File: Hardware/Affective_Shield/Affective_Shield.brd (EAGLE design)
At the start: 70 x 55 mm, 17 parts

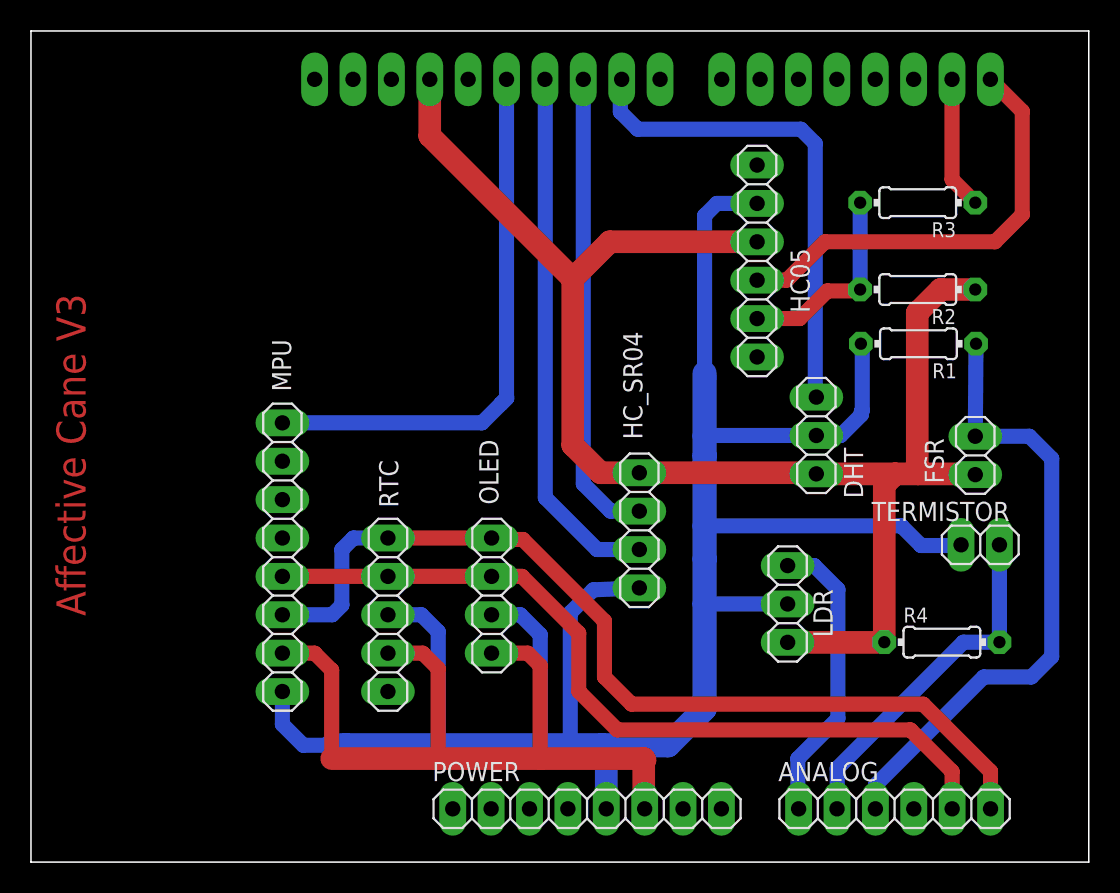
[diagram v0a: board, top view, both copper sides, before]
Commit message: Add Oximetry and GPS
Oximetry sensor added. GPS added
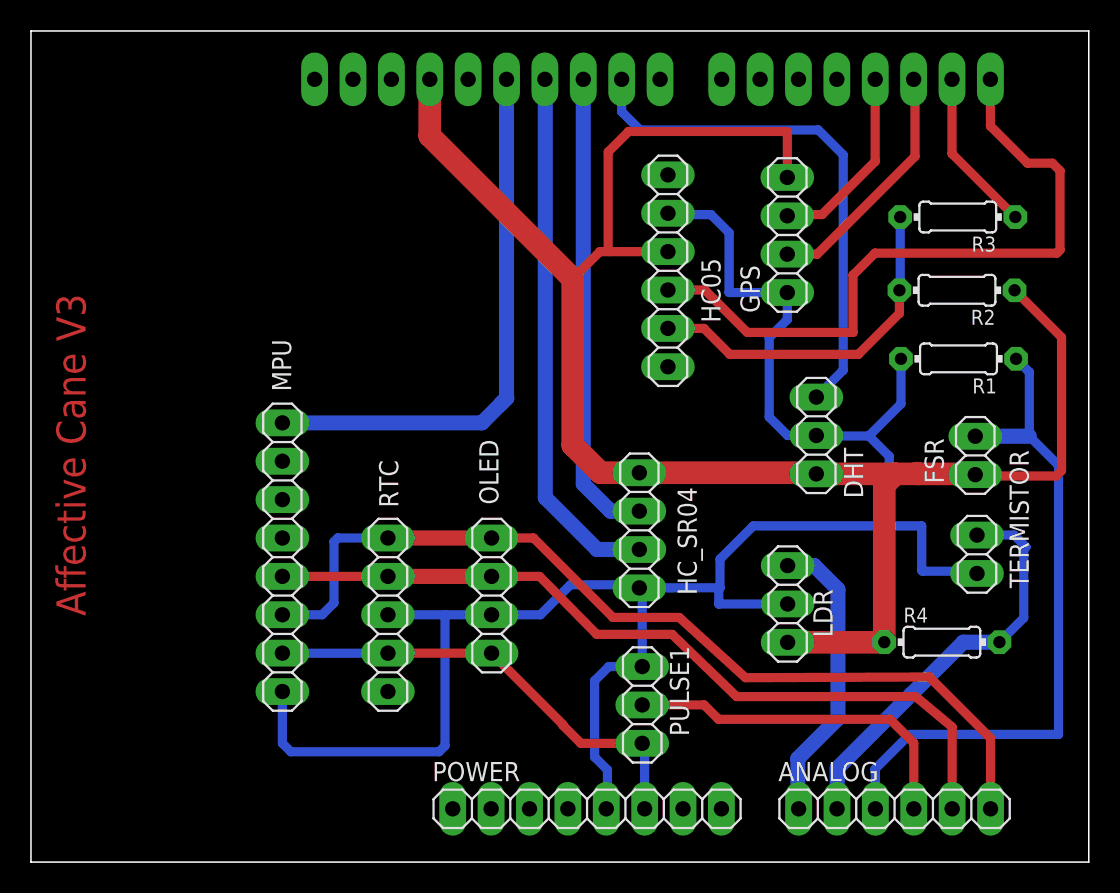
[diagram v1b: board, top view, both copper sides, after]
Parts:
- added GPS: GPS, pinhead:1X04
- added PULSE1: pulse_sensor, pinhead:1X03
- moved HC05 5.94 mm to (42.2, 38.1)
- moved R1 2.83 mm to (61.4, 32.3)
- moved R3 2.82 mm to (61.3, 41.7)
- moved R2 2.60 mm to (61.3, 36.8)
- moved TERMISTOR 0.66 mm to (62.6, 19.4), turned to 90 degrees
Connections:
- new net A3: ANALOG.4, PULSE1.2
- new net RX_GPS: GPS.2, JP1.3
- new net TX_GPS: GPS.3, JP1.4
- net +5V: now also GPS.1, PULSE1.1
- net GND1: now also PULSE1.3
- net GND2: now also GPS.4
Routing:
- net A3: track 0.00 -> 23.4 mm
- net GND1: track 53.3 -> 30.7 mm
- net GND2: track 101.8 -> 121.8 mm
- net +5V: track 150.6 -> 133.0 mm
- net RX: track 29.2 -> 45.8 mm
- net RX_GPS: track 0.00 -> 16.3 mm
- net TX_GPS: track 0.00 -> 12.7 mm
- net N$3: track 13.4 -> 23.5 mm
- net A1: track 23.3 -> 27.5 mm
- net A2: track 41.6 -> 45.3 mm
- net D09: track 32.8 -> 34.8 mm
- net TX: track 8.80 -> 10.8 mm
- net A4: track 54.4 -> 53.7 mm
- net A5: track 62.2 -> 61.6 mm

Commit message: shield corrective update: Changed some ports, and adapted to only bottom solder on components
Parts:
- removed R4: 10KR, resistor:0204/7
- removed TERMISTOR: TERMISTOR, pinhead:1X02
- added GSR_: GROOVE, pinhead:1X04
- moved LDR 2.02 mm to (51.9, 16.9), turned to 90 degrees
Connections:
- net +5V: now also GSR_.3; no longer TERMISTOR.1
- net A1: now also GSR_.1; no longer R4.2, TERMISTOR.2
- net A4: now also OLED.4; no longer OLED.3
- net A5: now also OLED.3; no longer OLED.4
- net GND1: now also GSR_.4
- net GND2: no longer R4.1
- net N$3: now also HC05.4; no longer HC05.5
- net RX: now also HC05.5; no longer HC05.4
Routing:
- net A5: track 61.6 -> 103.6 mm, vias 0 -> 3
- net GND1: track 30.7 -> 69.6 mm
- net GND2: track 121.8 -> 152.4 mm, vias 0 -> 4
- net +5V: track 133.0 -> 154.9 mm, vias 0 -> 5
- net A1: track 27.5 -> 17.1 mm
- net RX: track 45.8 -> 37.3 mm, vias 0 -> 2
- net A0: track 19.6 -> 12.3 mm
- net A4: track 53.7 -> 60.9 mm, vias 0 -> 7
- net D12: track 37.2 -> 34.5 mm, vias 0 -> 3
- net TX: track 10.8 -> 12.5 mm
- net D11: track 35.3 -> 34.6 mm, vias 0 -> 3
- net N$3: track 23.5 -> 22.9 mm, vias 0 -> 2
- net D09: track 34.8 -> 35.2 mm, vias 0 -> 2
- net A3: track 23.4 -> 23.6 mm, vias 0 -> 2
- net D10: track 31.2 -> 31.1 mm, vias 0 -> 3
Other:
- board text added: "Affective Cane V5"
- board text removed: "Affective Cane V3"
